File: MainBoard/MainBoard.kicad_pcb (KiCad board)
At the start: 2 copper layers, 33.8 x 131 mm, 81 parts, among them J1 Conn_02x04_Odd_Even, SW1 DSHP02TSGET, U1 W25Q16JVUXIQ, U10 VDMR10A1, U11 VDMR10A1, U12 VDMR10A1, U13 74LVC1G34GW,125, U14 SIP32431DR3-T1GE3, U2 RP2040, U3 IS31FL3729-QFLS4-TR, U4 VDMR10A1, U5 VDMR10A1, U6 VDMR10A1, U7 VDMR10A1, U8 VDMR10A1, U9 VDMR10A1, Y1 12.000MHz

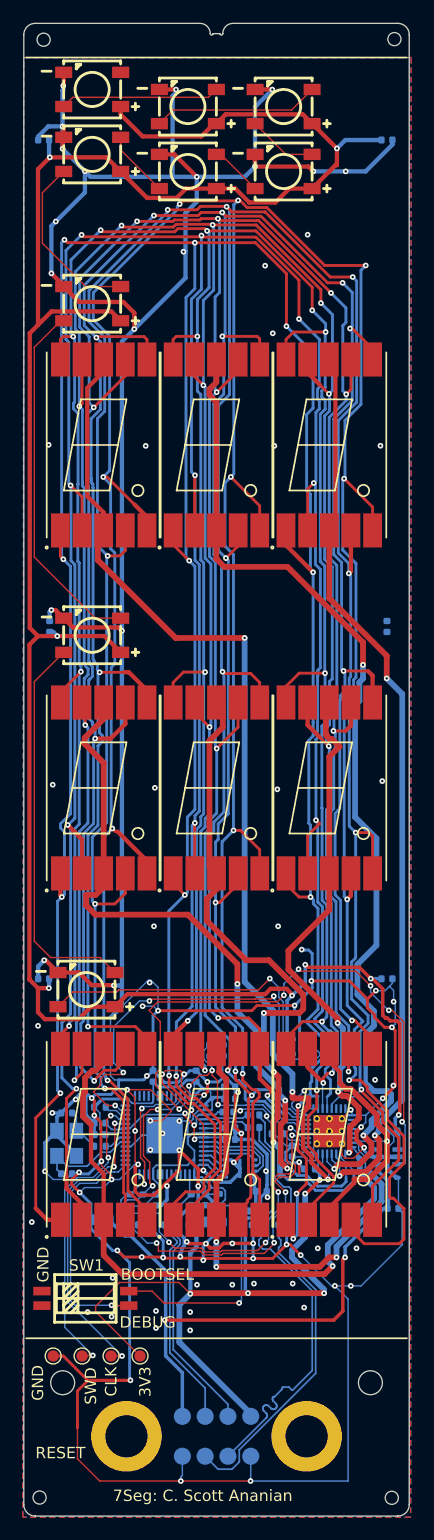
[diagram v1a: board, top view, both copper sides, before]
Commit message: Add Bezel PCB; adjust legend locations
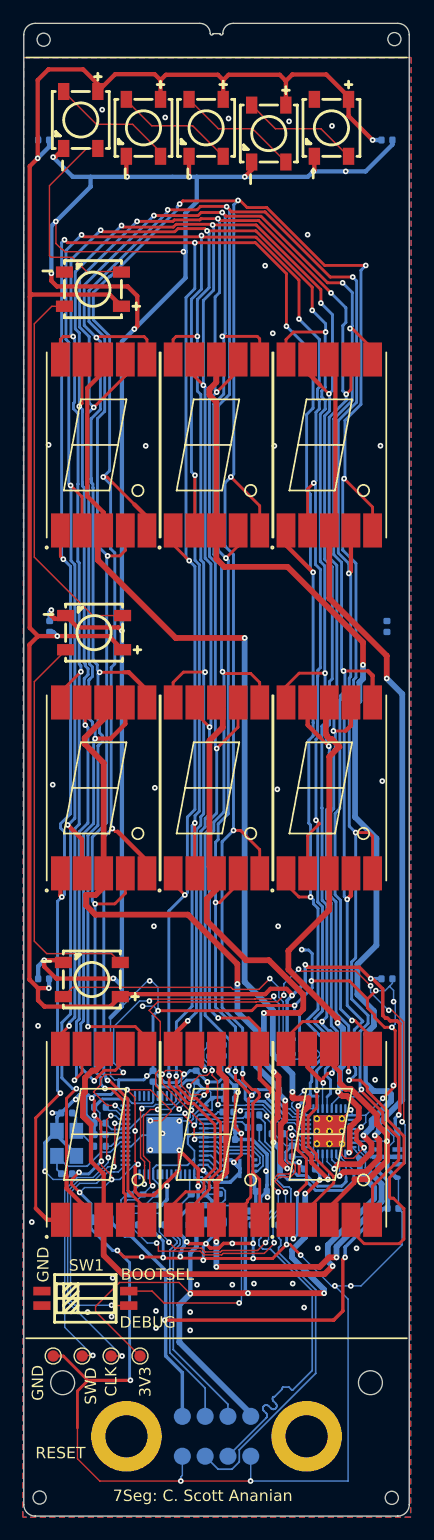
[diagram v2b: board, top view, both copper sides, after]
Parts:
- removed LED9: XL-5050RGBC-WS2812B, LCSC:LED-SMD_4P-L5.0-W5.0-BL_XL-5050RGBC
- moved LED8 12.7 mm to (77.0, 59.2), turned to 180 degrees
- moved LED6 7.80 mm to (66.0, 59.2), turned to 180 degrees
- moved LED5 5.47 mm to (60.5, 59.2), turned to 180 degrees
- moved LED4 3.18 mm to (55.0, 58.5), turned to 180 degrees
- moved LED7 2.70 mm to (71.5, 59.7), turned to 180 degrees
- moved LED3 1.27 mm to (56.1, 73.3)
- moved LED1 1.00 mm to (56.0, 133.9)
- moved LED2 0.28 mm to (56.2, 103.5)
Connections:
- LED8 pad 2: Net-(LED8-DOU) -> unconnected-(LED8-DOU-Pad2)
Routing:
- net Net-(LED8-DOU): track 14.0 -> 0.00 mm
- net GND: track 576.8 -> 567.3 mm, vias 113 -> 114
- net +5VP: track 209.2 -> 200.7 mm
- net Net-(LED5-DOU): track 4.64 -> 10.6 mm
- net Net-(LED4-DOU): track 5.91 -> 11.1 mm
- net Net-(LED6-DOU): track 6.12 -> 10.8 mm
- net Net-(LED7-DOU): track 14.6 -> 10.4 mm
- net Net-(LED3-DOU): track 15.5 -> 18.7 mm
- net Net-(LED2-DOU): track 31.8 -> 33.6 mm
- net /NEOPIXEL: track 27.0 -> 26.3 mm
- net Net-(LED1-DOU): track 34.6 -> 35.1 mm

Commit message: Optimize for manufacturability (use JLCPCB basic parts, etc)
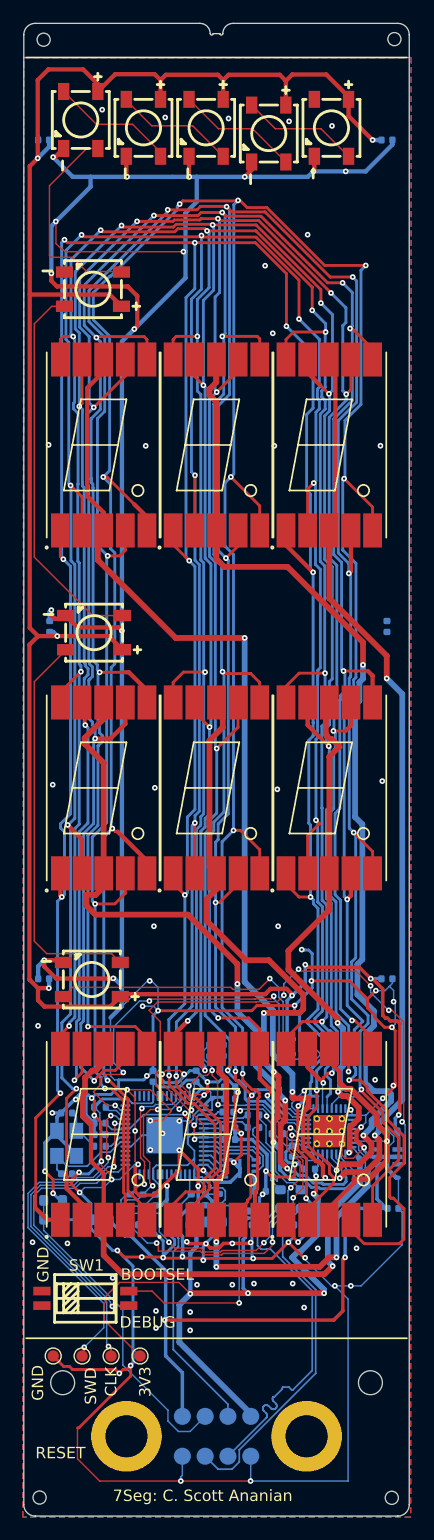
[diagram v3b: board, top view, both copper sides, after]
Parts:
- added R11: 5.1, Resistor_SMD:R_0603_1608Metric, B.Cu at (72.5, 153.2)
- added R13: 5.1, Resistor_SMD:R_0603_1608Metric, B.Cu at (74.3, 153.2)
- added R14: 470k, Resistor_SMD:R_0603_1608Metric, B.Cu at (52.6, 153.3)
- R5, R6: value 27 -> 22
- R7: value 180k -> 300k; footprint Resistor_SMD:R_0402_1005Metric -> Resistor_SMD:R_0603_1608Metric
- moved R7 9.29 mm to (52.6, 154.9), turned to 0 degrees
- moved D4 0.37 mm to (73.2, 155.4)
- moved C3 0.08 mm to (70.8, 152.5)
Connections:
- R5 pad 1: /USB_DP -> Net-(R11-Pad2)
- R6 pad 1: /USB_DN -> Net-(R13-Pad2)
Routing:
- net GND: track 567.3 -> 581.3 mm, vias 114 -> 115
- net /USB_DN: track 40.3 -> 30.7 mm
- net /BOARD_ID: track 18.9 -> 28.1 mm
- net Net-(R11-Pad2): track 0.00 -> 8.48 mm
- net Net-(R13-Pad2): track 0.00 -> 8.48 mm
- net /USB_DP: track 37.7 -> 30.7 mm
- net /SWD: track 27.1 -> 31.7 mm
- net /SWCLK: track 27.2 -> 30.2 mm
- net /Driver/CS4: track 313.3 -> 316.2 mm
- net /DEBUG_SW: track 20.6 -> 23.2 mm
- net +5V: track 52.5 -> 53.9 mm
- net /Driver/LED_SW6: track 54.0 -> 52.9 mm
- net /Driver/LED_SW7: track 43.7 -> 42.8 mm
- net /Driver/LED_SW1: track 89.7 -> 88.7 mm
- net /Driver/CS7: track 332.8 -> 332.0 mm

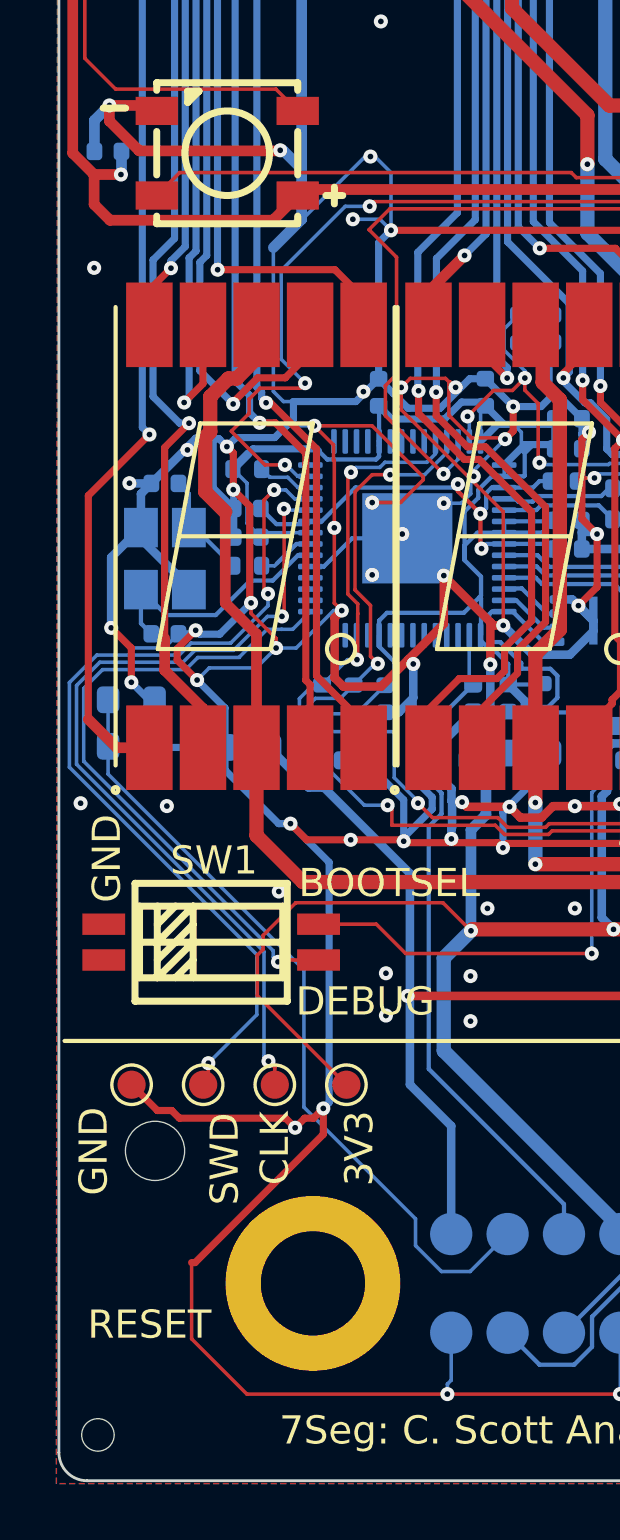
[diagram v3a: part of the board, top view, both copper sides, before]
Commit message: Add neopixel debugging header
This allows us to fab just the neopixels on the board, saving some cost
while we check to see how the backlight looks.
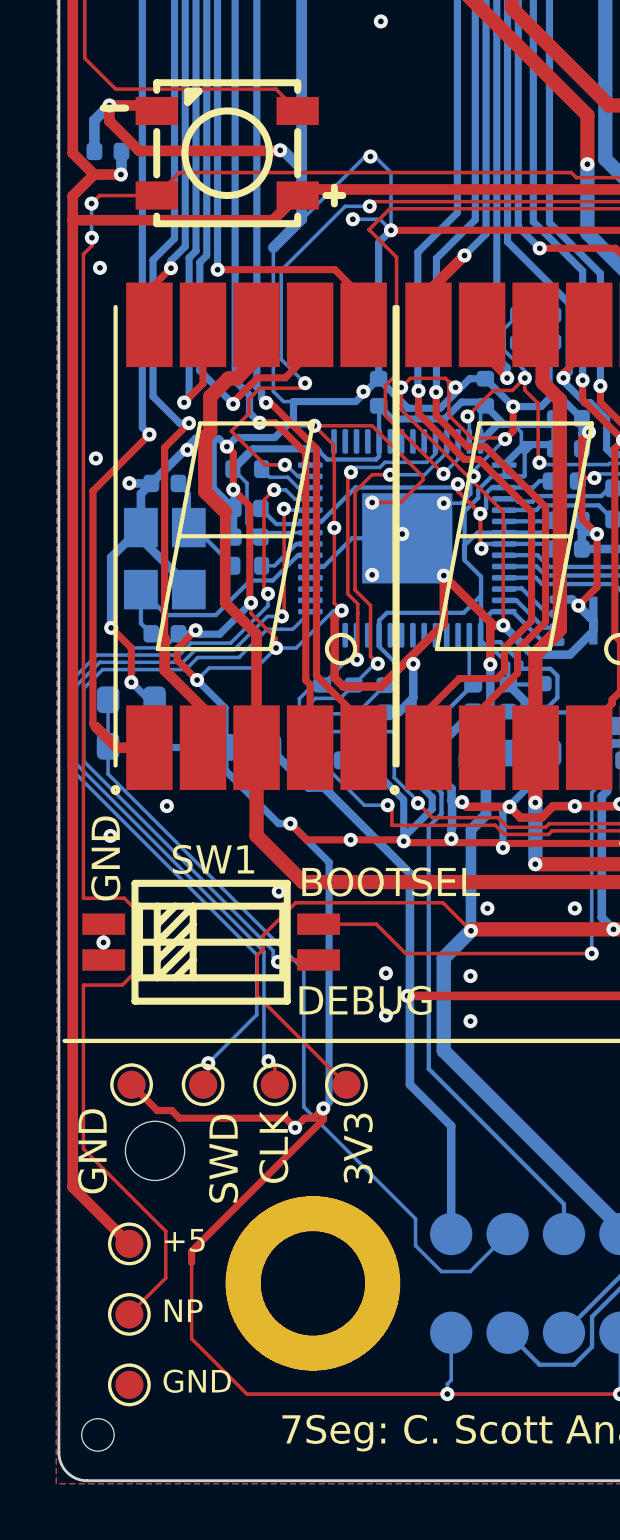
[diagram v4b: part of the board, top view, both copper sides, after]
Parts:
- added TP5: TestPoint, TestPoint:TestPoint_Pad_D1.0mm, F.Cu at (52.5, 172.6)
- added TP6: TestPoint, TestPoint:TestPoint_Pad_D1.0mm, F.Cu at (52.5, 175.1)
- added TP7: TestPoint, TestPoint:TestPoint_Pad_D1.0mm, F.Cu at (52.5, 177.6)
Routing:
- net /NEOPIXEL: track 26.3 -> 73.2 mm, vias 1 -> 3
- net +5VP: track 200.7 -> 239.2 mm
- net GND: track 581.3 -> 582.5 mm, vias 115 -> 117
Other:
- board text added: "+5"
- board text added: "NP"
- board text removed: "RESET"

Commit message: Switch Neopixel component type to match something JLCPCB is happy to assemble
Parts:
- LED1, LED2, LED3, LED4, LED5, LED6, LED7, LED8: value XL-5050RGBC-WS2812B -> SKC6812RGBW-BW-B
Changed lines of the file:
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@@
 			)
 		)
-		(property "Value" "XL-5050RGBC-WS2812B"
+		(property "Value" "SKC6812RGBW-BW-B"
 			(at 0 6.5 0)
 			(layer "F.Fab")
@@
 			)
 		)
-		(property "LCSC Part" "C2843785"
+		(property "LCSC Part" ""
+			(at 0 0 180)
+			(unlocked yes)
+			(layer "F.Fab")
+			(hide yes)
+			(effects
+				(font
+					(size 1 1)
+					(thickness 0.15)
+				)
+			)
+		)
+		(property "JLCPCB Rotation Offset" "90"
+			(at 0 0 180)
+			(unlocked yes)
+			(layer "F.Fab")
+			(hide yes)
+			(effects
+				(font
+					(size 1 1)
+					(thickness 0.15)
+				)
+			)
+		)
+		(property "LCSC" "C5380878"
 			(at 0 0 180)
 			(unlocked yes)
@@
 			)
 		)
-		(property "Value" "XL-5050RGBC-WS2812B"
+		(property "Value" "SKC6812RGBW-BW-B"
 			(at 0 6.5 90)
 			(layer "F.Fab")
@@
 			)
 		)
-		(property "LCSC Part" "C2843785"
+		(property "LCSC Part" ""
+			(at 0 0 90)
+			(unlocked yes)
+			(layer "F.Fab")
+			(hide yes)
+			(effects
+				(font
+					(size 1 1)
+					(thickness 0.15)
+				)
+			)
+		)
+		(property "JLCPCB Rotation Offset" "90"
+			(at 0 0 90)
+			(unlocked yes)
+			(layer "F.Fab")
+			(hide yes)
+			(effects
+				(font
+					(size 1 1)
+					(thickness 0.15)
+				)
+			)
+		)
+		(property "LCSC" "C5380878"
 			(at 0 0 90)
 			(unlocked yes)
@@
 			)
 		)
-		(property "Value" "XL-5050RGBC-WS2812B"
+		(property "Value" "SKC6812RGBW-BW-B"
 			(at 0 6.5 90)
 			(layer "F.Fab")
@@
 			)
 		)
-		(property "LCSC Part" "C2843785"
+		(property "LCSC Part" ""
+			(at 0 0 90)
+			(unlocked yes)
+			(layer "F.Fab")
+			(hide yes)
+			(effects
+				(font
+					(size 1 1)
+					(thickness 0.15)
+				)
+			)
+		)
+		(property "JLCPCB Rotation Offset" "90"
+			(at 0 0 90)
+			(unlocked yes)
+			(layer "F.Fab")
+			(hide yes)
+			(effects
+				(font
+					(size 1 1)
+					(thickness 0.15)
+				)
+			)
+		)
+		(property "LCSC" "C5380878"
 			(at 0 0 90)
 			(unlocked yes)
@@
 			)
 		)
-		(property "Value" "XL-5050RGBC-WS2812B"
+		(property "Value" "SKC6812RGBW-BW-B"
 			(at 0 6.5 90)
 			(layer "F.Fab")
@@
 			)
 		)
-		(property "LCSC Part" "C2843785"
+		(property "LCSC Part" ""
+			(at 0 0 90)
+			(unlocked yes)
+			(layer "F.Fab")
+			(hide yes)
+			(effects
+				(font
+					(size 1 1)
+					(thickness 0.15)
+				)
+			)
+		)
+		(property "JLCPCB Rotation Offset" "90"
+			(at 0 0 90)
+			(unlocked yes)
+			(layer "F.Fab")
+			(hide yes)
+			(effects
+				(font
+					(size 1 1)
+					(thickness 0.15)
+				)
+			)
+		)
+		(property "LCSC" "C5380878"
 			(at 0 0 90)
 			(unlocked yes)
@@
 			)
 		)
-		(property "Value" "XL-5050RGBC-WS2812B"
+		(property "Value" "SKC6812RGBW-BW-B"
 			(at 0 6.5 0)
 			(layer "F.Fab")
@@
 			)
 		)
-		(property "LCSC Part" "C2843785"
+		(property "LCSC Part" ""
+			(at 0 0 180)
+			(unlocked yes)
+			(layer "F.Fab")
+			(hide yes)
+			(effects
+				(font
+					(size 1 1)
+					(thickness 0.15)
+				)
+			)
+		)
+		(property "JLCPCB Rotation Offset" "90"
+			(at 0 0 180)
+			(unlocked yes)
+			(layer "F.Fab")
+			(hide yes)
+			(effects
+				(font
+					(size 1 1)
+					(thickness 0.15)
+				)
+			)
+		)
+		(property "LCSC" "C5380878"
 			(at 0 0 180)
 			(unlocked yes)
@@
 			)
 		)
-		(property "Value" "XL-5050RGBC-WS2812B"
+		(property "Value" "SKC6812RGBW-BW-B"
 			(at 0 6.5 0)
 			(layer "F.Fab")
@@
 			)
 		)
-		(property "LCSC Part" "C2843785"
+		(property "LCSC Part" ""
+			(at 0 0 180)
+			(unlocked yes)
+			(layer "F.Fab")
+			(hide yes)
+			(effects
+				(font
+					(size 1 1)
+					(thickness 0.15)
+				)
+			)
+		)
+		(property "JLCPCB Rotation Offset" "90"
+			(at 0 0 180)
+			(unlocked yes)
+			(layer "F.Fab")
+			(hide yes)
+			(effects
+				(font
+					(size 1 1)
+					(thickness 0.15)
+				)
+			)
+		)
+		(property "LCSC" "C5380878"
 			(at 0 0 180)
 			(unlocked yes)
@@
 			)
 		)
-		(property "Value" "XL-5050RGBC-WS2812B"
+		(property "Value" "SKC6812RGBW-BW-B"
 			(at 0 6.5 0)
 			(layer "F.Fab")
@@
 			)
 		)
-		(property "LCSC Part" "C2843785"
+		(property "LCSC Part" ""
+			(at 0 0 180)
+			(unlocked yes)
+			(layer "F.Fab")
+			(hide yes)
+			(effects
+				(font
+					(size 1 1)
+					(thickness 0.15)
+				)
+			)
+		)
+		(property "JLCPCB Rotation Offset" "90"
+			(at 0 0 180)
+			(unlocked yes)
+			(layer "F.Fab")
+			(hide yes)
+			(effects
+				(font
+					(size 1 1)
+					(thickness 0.15)
+				)
+			)
+		)
+		(property "LCSC" "C5380878"
 			(at 0 0 180)
 			(unlocked yes)
@@
 			)
 		)
-		(property "Value" "XL-5050RGBC-WS2812B"
+		(property "Value" "SKC6812RGBW-BW-B"
 			(at 0 6.5 0)
 			(layer "F.Fab")
@@
 			)
 		)
-		(property "LCSC Part" "C2843785"
+		(property "LCSC Part" ""
+			(at 0 0 180)
+			(unlocked yes)
+			(layer "F.Fab")
+			(hide yes)
+			(effects
+				(font
+					(size 1 1)
+					(thickness 0.15)
+				)
+			)
+		)
+		(property "JLCPCB Rotation Offset" "90"
+			(at 0 0 180)
+			(unlocked yes)
+			(layer "F.Fab")
+			(hide yes)
+			(effects
+				(font
+					(size 1 1)
+					(thickness 0.15)
+				)
+			)
+		)
+		(property "LCSC" "C5380878"
 			(at 0 0 180)
 			(unlocked yes)
